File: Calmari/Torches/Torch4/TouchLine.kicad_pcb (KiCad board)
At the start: 2 copper layers, 89 x 12 mm, 18 parts

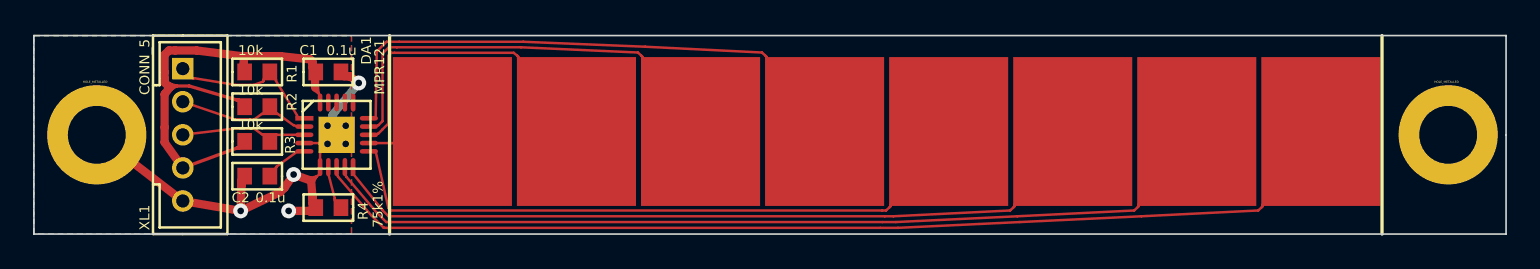
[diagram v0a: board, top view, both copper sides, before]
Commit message: 
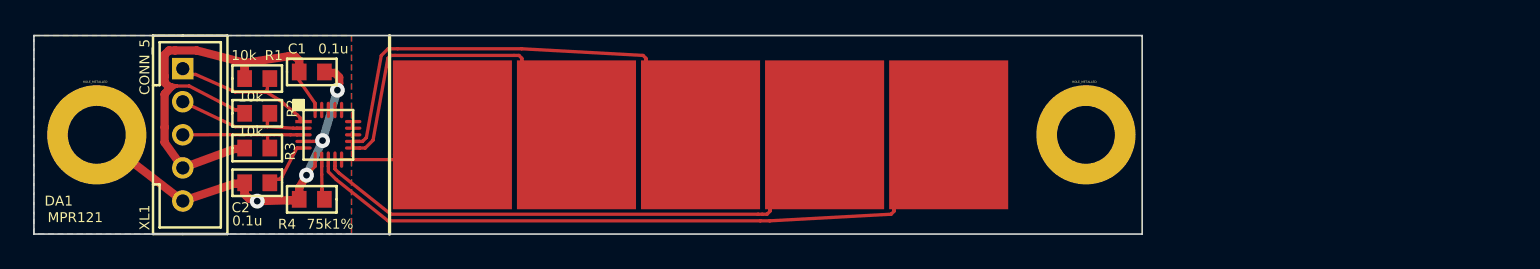
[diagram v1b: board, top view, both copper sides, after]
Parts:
- removed SNSP6, SNSP7, SNSP8: SENSORPAD, SENSOR_PAD_7D2_9
- DA1: footprint QFN20 -> QFN20_04PITCH
- moved SNSP3 37.5 mm to (94.8, 74.0)
- moved SNSP1 22.5 mm to (124.8, 74.0)
- moved SNSP2 22.5 mm to (117.3, 74.0)
- moved SNSP4 22.5 mm to (102.3, 74.0)
- moved HOLE1 21.9 mm to (133.1, 74.0)
- moved SNSP5 15.0 mm to (109.8, 74.0)
- moved R4 1.12 mm to (86.3, 77.9)
- moved C1 1.00 mm to (86.3, 70.2)
- moved DA1 0.50 mm to (87.3, 74.0)
- moved C2 0.40 mm to (83.0, 76.9)
- moved R2 0.40 mm to (83.0, 72.7)
- moved R1 0.40 mm to (83.0, 70.6)
- moved R3 0.40 mm to (83.0, 74.8)
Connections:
- DA1 pad 13: N-000004 -> (no net)
- DA1 pad 14: N-000006 (its old number) -> (no net)
- DA1 pad 15: N-0000013 -> (no net)
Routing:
- net N-000008: track 47.5 -> 7.32 mm
- net N-0000013: track 34.1 -> 0.00 mm
- net N-000006 (its old number): track 26.7 -> 0.00 mm
- net N-0000012: track 5.12 -> 27.9 mm
- net N-000007: track 55.6 -> 33.6 mm
- net N-000006: track 63.8 -> 41.8 mm
- net N-0000016: track 40.2 -> 20.4 mm
- net N-000004: track 19.3 -> 0.00 mm
- net GND: track 30.3 -> 25.8 mm
- net +3.3V: track 30.6 -> 29.7 mm
- net N-000001: track 2.71 -> 3.21 mm
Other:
- board size 89 x 12 mm -> 67 x 12 mm
